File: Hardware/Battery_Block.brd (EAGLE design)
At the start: 30.5 x 44.5 mm, 24 parts, among them U1 MCP73831, U2 EDISON_CONNECTOR_FULLMOUNTING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, U3 EDISON_CONNECTOR_FULLHEADER

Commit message: file cleanup
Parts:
- JP1: value USB_MICROB_PLUGCONN-11752 -> USB_MICROB_PLUG
- SJ1: value JUMPER-PAD-2-NC_BY_TRACE -> LED DISABLE
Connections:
- net N$1 renamed VIN
- net N$6 renamed VBAT
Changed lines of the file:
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@@
 <element name="FID1" library="SparkFun-Aesthetics" package="FIDUCIAL-1X2" value="FIDUCIAL1X2" x="3.81" y="5.08"/>
 <element name="FID2" library="SparkFun-Aesthetics" package="FIDUCIAL-1X2" value="FIDUCIAL1X2" x="25.4" y="43.18"/>
-<element name="JP1" library="SparkFun-Connectors" package="USB-B-MICRO-SMD_V03" value="USB_MICROB_PLUGCONN-11752" x="15.24" y="42.291" rot="R270">
+<element name="JP1" library="SparkFun-Connectors" package="USB-B-MICRO-SMD_V03" value="USB_MICROB_PLUG" x="15.24" y="42.291" rot="R270">
 <attribute name="PROD_ID" value="CONN-11752" x="15.24" y="42.291" size="1.778" layer="27" rot="R270" display="off"/>
 </element>
@@
 <attribute name="PROD_ID" value="RES-07856" x="1.016" y="6.35" size="0.8128" layer="27" font="vector" ratio="15" rot="R270" display="off"/>
 </element>
-<element name="SJ1" library="SparkFun-Passives" package="PAD-JUMPER-2-NC_BY_TRACE_YES_SILK" value="JUMPER-PAD-2-NC_BY_TRACE" x="3.048" y="15.748" rot="R90"/>
+<element name="SJ1" library="SparkFun-Passives" package="PAD-JUMPER-2-NC_BY_TRACE_YES_SILK" value="LED DISABLE" x="3.048" y="15.748" rot="R90"/>
 <element name="FID3" library="SparkFun-Aesthetics" package="FIDUCIAL-1X2" value="FIDUCIAL1X2" x="3.81" y="5.08" rot="MR0"/>
 <element name="FID4" library="SparkFun-Aesthetics" package="FIDUCIAL-1X2" value="FIDUCIAL1X2" x="25.4" y="43.18" rot="MR0"/>
@@
 <contactref element="U3" pad="67"/>
 </signal>
-<signal name="N$1">
+<signal name="VIN">
 <contactref element="JP1" pad="VBUS1"/>
 <contactref element="U1" pad="4"/>
@@
 <wire x1="2.794" y1="36.715" x2="1.016" y2="34.937" width="0.4064" layer="1"/>
 </signal>
-<signal name="N$6">
+<signal name="VBAT">
 <contactref element="U1" pad="3"/>
 <contactref element="C2" pad="1"/>

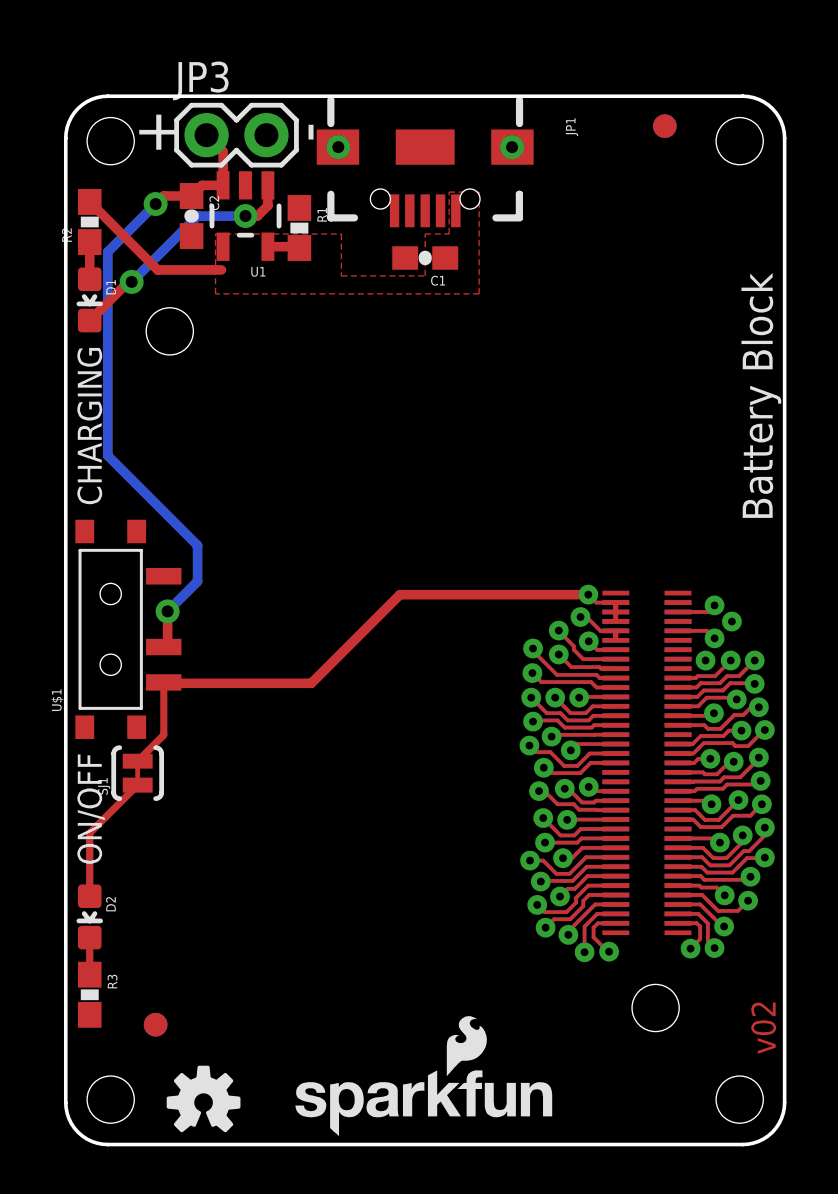
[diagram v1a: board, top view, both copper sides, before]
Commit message: Fix text rotation, go to v10
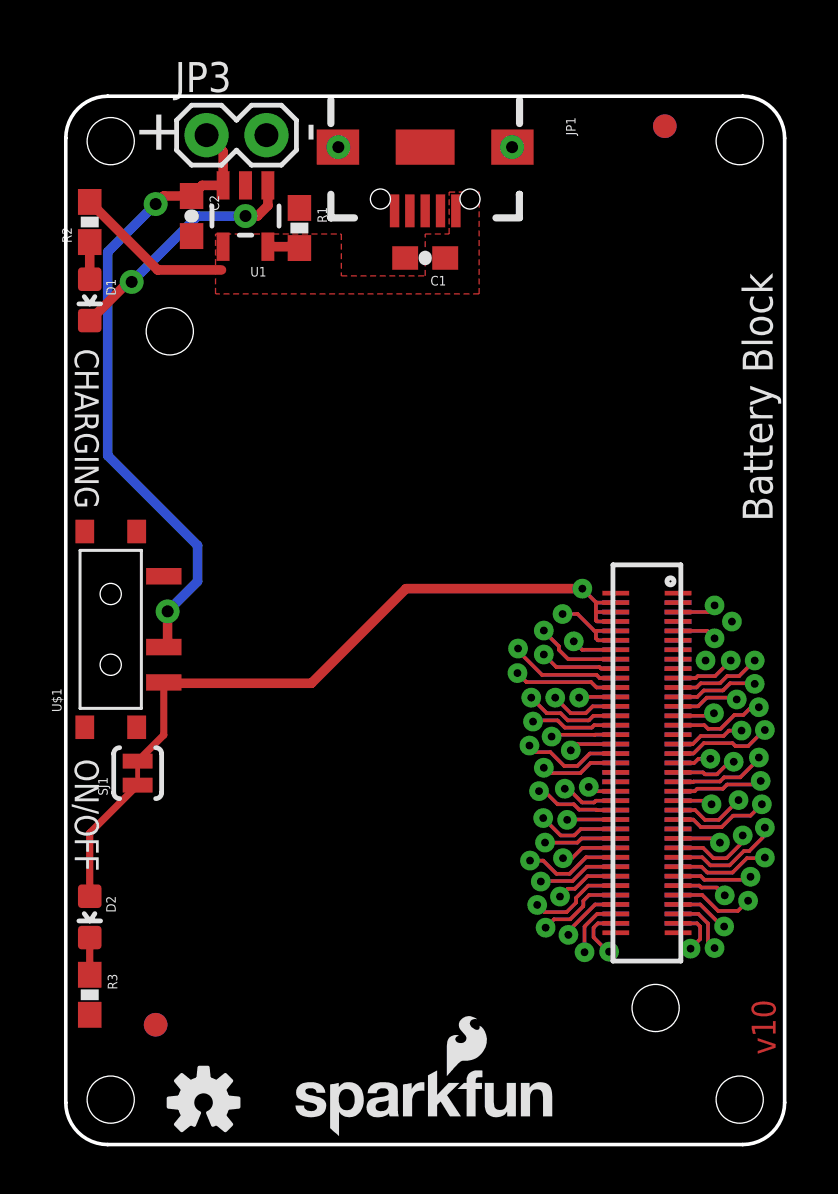
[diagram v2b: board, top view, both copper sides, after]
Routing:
- net VSYS: track 28.0 -> 31.6 mm
- net 3.3V: track 4.47 -> 7.49 mm
- net USB_VBUS: track 7.57 -> 8.84 mm
- net USB_DN: track 8.17 -> 9.44 mm
- net 1.8V: track 2.95 -> 4.22 mm
- net DCIN: track 6.05 -> 7.32 mm
- net USB_DP: track 5.33 -> 6.60 mm
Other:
- board text added: "v10"
- board text removed: "v02"

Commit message: Add some silk, update fp, ready for reds
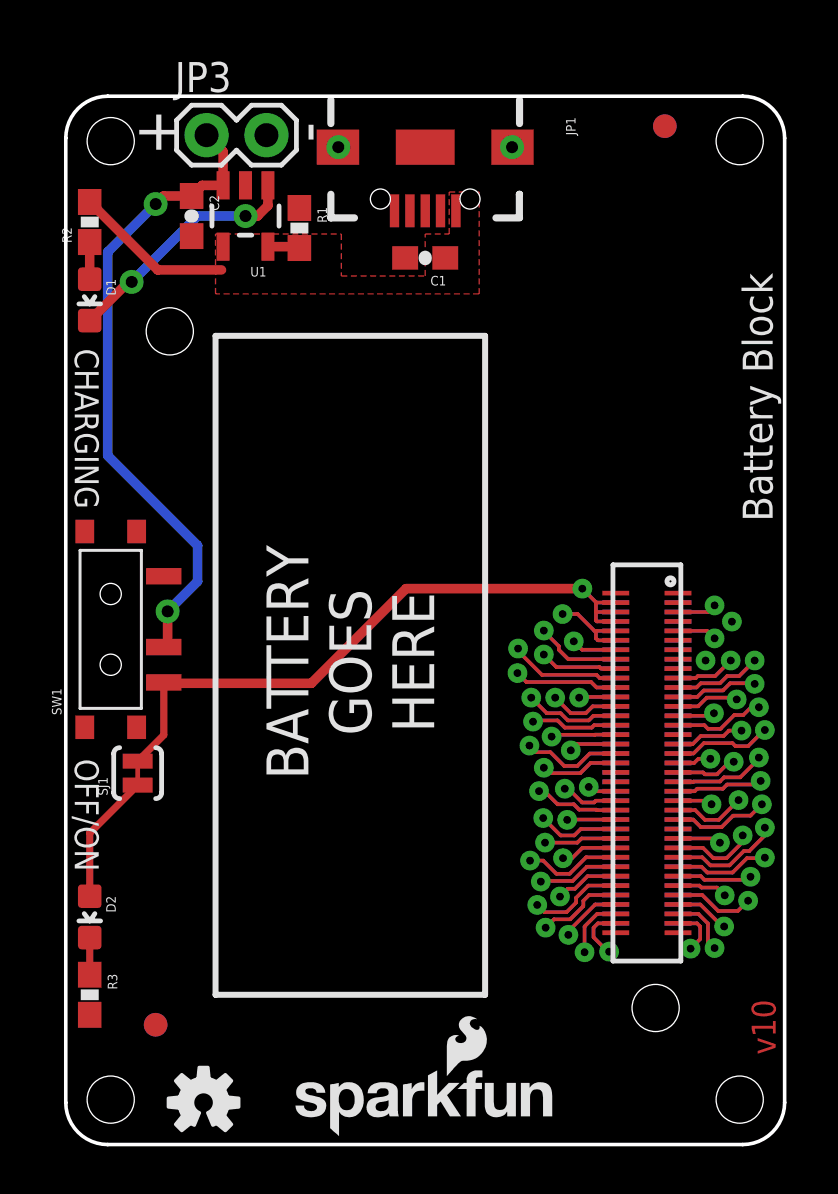
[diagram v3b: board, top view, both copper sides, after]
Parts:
- renumbered U$1 to SW1
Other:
- board text added: "BATTERY GOES HERE"
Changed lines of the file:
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@@
 <grid distance="0.05" unitdist="inch" unit="inch" style="lines" multiple="1" display="yes" altdistance="0.005" altunitdist="inch" altunit="inch"/>
 <layers>
-<layer number="1" name="Top" color="4" fill="1" visible="no" active="yes"/>
+<layer number="1" name="Top" color="4" fill="1" visible="yes" active="yes"/>
 <layer number="2" name="Route2" color="1" fill="3" visible="no" active="yes"/>
 <layer number="15" name="Route15" color="4" fill="6" visible="no" active="yes"/>
@@
 <layer number="19" name="Unrouted" color="6" fill="1" visible="yes" active="yes"/>
 <layer number="20" name="Dimension" color="15" fill="1" visible="yes" active="yes"/>
-<layer number="21" name="tPlace" color="16" fill="1" visible="no" active="yes"/>
+<layer number="21" name="tPlace" color="16" fill="1" visible="yes" active="yes"/>
 <layer number="22" name="bPlace" color="14" fill="1" visible="yes" active="yes"/>
-<layer number="23" name="tOrigins" color="15" fill="1" visible="no" active="yes"/>
+<layer number="23" name="tOrigins" color="15" fill="1" visible="yes" active="yes"/>
 <layer number="24" name="bOrigins" color="15" fill="1" visible="yes" active="yes"/>
 <layer number="25" name="tNames" color="7" fill="1" visible="no" active="yes"/>
@@
 <layer number="43" name="vRestrict" color="2" fill="10" visible="no" active="yes"/>
 <layer number="44" name="Drills" color="7" fill="1" visible="no" active="yes"/>
-<layer number="45" name="Holes" color="7" fill="1" visible="no" active="yes"/>
+<layer number="45" name="Holes" color="7" fill="1" visible="yes" active="yes"/>
 <layer number="46" name="Milling" color="3" fill="1" visible="no" active="yes"/>
-<layer number="51" name="tDocu" color="6" fill="1" visible="no" active="yes"/>
+<layer number="51" name="tDocu" color="6" fill="1" visible="yes" active="yes"/>
 <layer number="3" name="Route3" color="4" fill="3" visible="no" active="no"/>
 <layer number="4" name="Route4" color="1" fill="4" visible="no" active="no"/>
@@
 <text x="30.099" y="3.81" size="1.016" layer="1" font="vector" ratio="15" rot="R90">v10</text>
 <text x="0.889" y="30.353" size="1.016" layer="21" font="vector" ratio="15" rot="SR270" align="center">CHARGING</text>
-<text x="0.889" y="13.97" size="1.016" layer="21" font="vector" ratio="15" rot="SR270" align="center">ON/OFF</text>
-<text x="0.762" y="22.098" size="0.8128" layer="22" font="vector" ratio="15" rot="SMR90" align="center">OFF/ON</text>
+<text x="0.889" y="13.97" size="1.016" layer="21" font="vector" ratio="15" rot="SR270" align="center">OFF/ON</text>
+<text x="0.762" y="22.098" size="0.8128" layer="22" font="vector" ratio="15" rot="SMR90" align="center">ON/OFF</text>
 <text x="3.81" y="42.926" size="1.9304" layer="21" font="vector" ratio="15" rot="R90" align="center">+</text>
 <text x="5.842" y="40.64" size="1.9304" layer="22" font="vector" ratio="15" rot="MR0" align="center">+</text>
@@
 <text x="29.972" y="39.878" size="1.27" layer="22" font="vector" ratio="15" rot="SMR270">Battery Block</text>
 <text x="31.75" y="-2.54" size="1.778" layer="51">Note: Units are in Inches</text>
+<wire x1="17.78" y1="34.29" x2="6.35" y2="34.29" width="0.254" layer="21"/>
+<wire x1="6.35" y1="34.29" x2="6.35" y2="6.35" width="0.254" layer="21"/>
+<wire x1="6.35" y1="6.35" x2="17.78" y2="6.35" width="0.254" layer="21"/>
+<wire x1="17.78" y1="6.35" x2="17.78" y2="34.29" width="0.254" layer="21"/>
+<text x="12.065" y="20.447" size="1.778" layer="21" font="vector" ratio="15" rot="R90" align="center">BATTERY
+GOES
+HERE</text>
 </plain>
 <attributes>
@@
 <attribute name="PROD_ID" value="CAP-08280" x="15.24" y="37.592" size="1.778" layer="27" rot="R180" display="off"/>
 </element>
-<element name="U$1" library="SparkFun-Electromechanical" package="KPS-1290" value="SWITCH_SPDT" x="1.905" y="21.844" rot="R270">
+<element name="SW1" library="SparkFun-Electromechanical" package="KPS-1290" value="SWITCH_SPDT" x="1.905" y="21.844" rot="R270">
 <attribute name="PROD_ID" value="SWCH-10651" x="1.905" y="21.844" size="1.778" layer="27" rot="R270" display="off"/>
 </element>
@@
 <contactref element="U3" pad="2"/>
 <contactref element="U3" pad="4"/>
-<contactref element="U$1" pad="S"/>
+<contactref element="SW1" pad="S"/>
 <wire x1="14.4266" y1="23.5706" x2="10.414" y2="19.558" width="0.4064" layer="1"/>
 <wire x1="10.414" y1="19.558" x2="4.191" y2="19.558" width="0.4064" layer="1"/>
@@
 <contactref element="C2" pad="1"/>
 <contactref element="JP3" pad="1"/>
-<contactref element="U$1" pad="P"/>
+<contactref element="SW1" pad="P"/>
 <wire x1="6.67" y1="40.6701" x2="6.67" y2="42.098" width="0.4064" layer="1"/>
 <wire x1="6.67" y1="42.098" x2="5.969" y2="42.799" width="0.4064" layer="1"/>
@@
 </board>
 </drawing>
+<compatibility>
+<note version="6.3" minversion="6.2.2" severity="warning">
+Since Version 6.2.2 text objects can contain more than one line,
+which will not be processed correctly with this version.
+</note>
+</compatibility>
 </eagle>

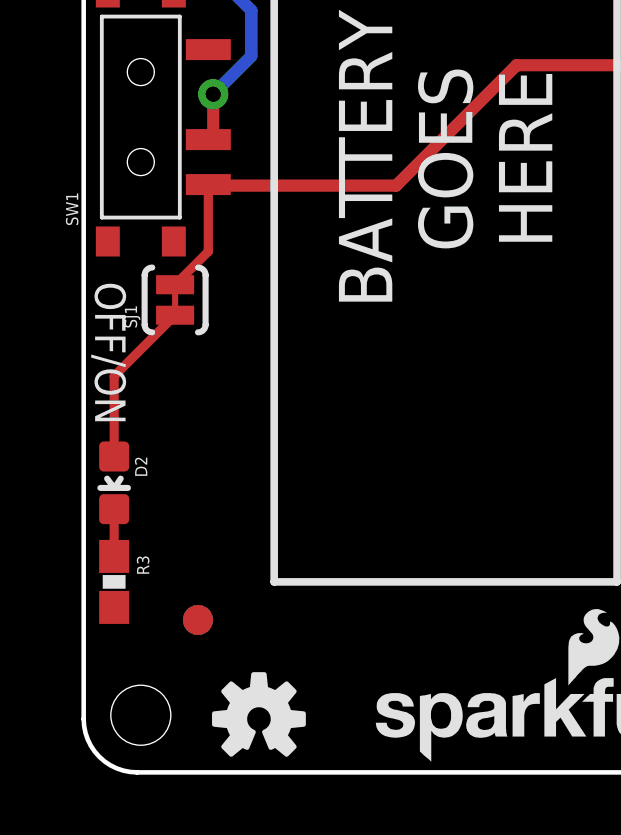
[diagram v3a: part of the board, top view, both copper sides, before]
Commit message: Ready for reds. Tweaked some silk positions, jumper position, on/off nomenclature No known to-do items
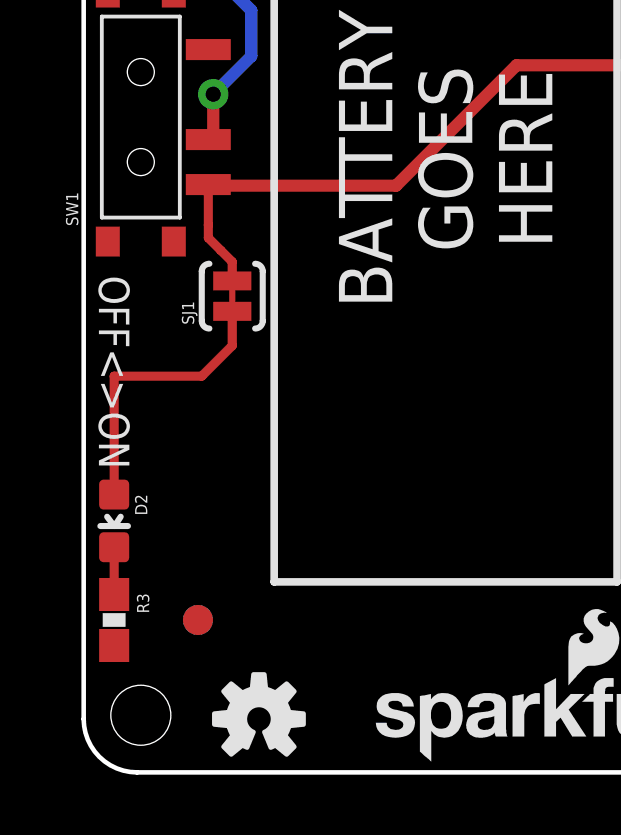
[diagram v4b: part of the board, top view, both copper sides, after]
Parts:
- moved SJ1 1.91 mm to (4.95, 15.9)
- moved D2 1.27 mm to (1.02, 8.38)
- moved R3 1.27 mm to (1.02, 5.08)
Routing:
- net N$7: track 5.55 -> 9.45 mm
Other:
- board text added: "OFF<>ON"
- board text added: "ON<>OFF"
- board text removed: "OFF/ON"
- board text removed: "ON/OFF"
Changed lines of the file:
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@@
 <text x="30.099" y="3.81" size="1.016" layer="1" font="vector" ratio="15" rot="R90">v10</text>
 <text x="0.889" y="30.353" size="1.016" layer="21" font="vector" ratio="15" rot="SR270" align="center">CHARGING</text>
-<text x="0.889" y="13.97" size="1.016" layer="21" font="vector" ratio="15" rot="SR270" align="center">OFF/ON</text>
-<text x="0.762" y="22.098" size="0.8128" layer="22" font="vector" ratio="15" rot="SMR90" align="center">ON/OFF</text>
+<text x="1.016" y="13.335" size="1.016" layer="21" font="vector" ratio="15" rot="SR270" align="center">OFF&lt;&gt;ON</text>
+<text x="0.762" y="22.098" size="0.8128" layer="22" font="vector" ratio="15" rot="SMR90" align="center">ON&lt;&gt;OFF</text>
 <text x="3.81" y="42.926" size="1.9304" layer="21" font="vector" ratio="15" rot="R90" align="center">+</text>
 <text x="5.842" y="40.64" size="1.9304" layer="22" font="vector" ratio="15" rot="MR0" align="center">+</text>
@@
 <attribute name="PROD_ID" value="CAP-08280" x="5.334" y="39.37" size="1.778" layer="27" rot="R270" display="off"/>
 </element>
-<element name="D2" library="SparkFun-LED" package="LED-0603" value="BLUE" x="1.016" y="9.652" rot="R180">
-<attribute name="PROD_ID" value="DIO-08575" x="1.016" y="9.652" size="0.8128" layer="27" font="vector" ratio="15" rot="R180" display="off"/>
+<element name="D2" library="SparkFun-LED" package="LED-0603" value="BLUE" x="1.016" y="8.382" rot="R180">
+<attribute name="PROD_ID" value="DIO-08575" x="1.016" y="8.382" size="0.8128" layer="27" font="vector" ratio="15" rot="R180" display="off"/>
 </element>
-<element name="R3" library="SparkFun-Resistors" package="0603-RES" value="1k" x="1.016" y="6.35" rot="R270">
-<attribute name="PROD_ID" value="RES-07856" x="1.016" y="6.35" size="0.8128" layer="27" font="vector" ratio="15" rot="R270" display="off"/>
+<element name="R3" library="SparkFun-Resistors" package="0603-RES" value="1k" x="1.016" y="5.08" rot="R270">
+<attribute name="PROD_ID" value="RES-07856" x="1.016" y="5.08" size="0.8128" layer="27" font="vector" ratio="15" rot="R270" display="off"/>
 </element>
-<element name="SJ1" library="SparkFun-Passives" package="PAD-JUMPER-2-NC_BY_TRACE_YES_SILK" value="LED DISABLE" x="3.048" y="15.748" rot="R90"/>
+<element name="SJ1" library="SparkFun-Passives" package="PAD-JUMPER-2-NC_BY_TRACE_YES_SILK" value="LED DISABLE" x="4.953" y="15.875" rot="R90"/>
 <element name="FID3" library="SparkFun-Aesthetics" package="FIDUCIAL-1X2" value="FIDUCIAL1X2" x="3.81" y="5.08" rot="MR0"/>
 <element name="FID4" library="SparkFun-Aesthetics" package="FIDUCIAL-1X2" value="FIDUCIAL1X2" x="25.4" y="43.18" rot="MR0"/>
@@
 <wire x1="4.191" y1="19.558" x2="4.155" y2="19.594" width="0.4064" layer="1"/>
 <contactref element="SJ1" pad="2"/>
-<wire x1="3.048" y1="16.256" x2="4.155" y2="17.363" width="0.3048" layer="1"/>
-<wire x1="4.155" y1="17.363" x2="4.155" y2="19.594" width="0.3048" layer="1"/>
+<wire x1="4.953" y1="16.383" x2="4.953" y2="17.018" width="0.3048" layer="1"/>
+<wire x1="4.953" y1="17.018" x2="4.572" y2="17.399" width="0.3048" layer="1"/>
+<wire x1="4.155" y1="18.252" x2="4.155" y2="19.594" width="0.3048" layer="1"/>
 <wire x1="21.9022" y1="23.5706" x2="22.493" y2="22.9798" width="0.1524" layer="16"/>
 <wire x1="22.493" y1="22.9798" x2="23.32" y2="22.9798" width="0.1524" layer="16"/>
@@
 <wire x1="23.32" y1="22.5798" x2="22.5052" y2="22.5798" width="0.1524" layer="1"/>
 <wire x1="22.5052" y1="22.5798" x2="22.479" y2="22.606" width="0.1524" layer="1"/>
+<wire x1="4.572" y1="17.399" x2="4.155" y2="17.816" width="0.3048" layer="1"/>
+<wire x1="4.155" y1="18.252" x2="4.155" y2="17.816" width="0.3048" layer="1"/>
 </signal>
 <signal name="3.3V">
@@
 <contactref element="D2" pad="C"/>
 <contactref element="R3" pad="1"/>
-<wire x1="1.016" y1="8.775" x2="1.016" y2="7.2" width="0.3048" layer="1"/>
+<wire x1="1.016" y1="7.505" x2="1.016" y2="5.93" width="0.3048" layer="1"/>
 </signal>
 <signal name="N$7">
 <contactref element="D2" pad="A"/>
 <contactref element="SJ1" pad="1"/>
-<wire x1="1.016" y1="10.529" x2="1.016" y2="13.208" width="0.3048" layer="1"/>
-<wire x1="1.016" y1="13.208" x2="3.048" y2="15.24" width="0.3048" layer="1"/>
+<wire x1="1.016" y1="9.259" x2="1.016" y2="13.208" width="0.3048" layer="1"/>
+<wire x1="1.016" y1="13.208" x2="3.937" y2="13.208" width="0.3048" layer="1"/>
+<wire x1="3.937" y1="13.208" x2="4.953" y2="14.224" width="0.3048" layer="1"/>
+<wire x1="4.953" y1="14.224" x2="4.953" y2="15.367" width="0.3048" layer="1"/>
 </signal>
 <signal name="DCIN">
